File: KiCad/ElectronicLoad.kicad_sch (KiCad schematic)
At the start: 180 parts, among them J1 LOAD, J2 SMA2, J3 SMA1, J4 12V, J5 USB, J6 PROG, M1 FAN, Q1 any, Q2 any, Q3 BSS138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

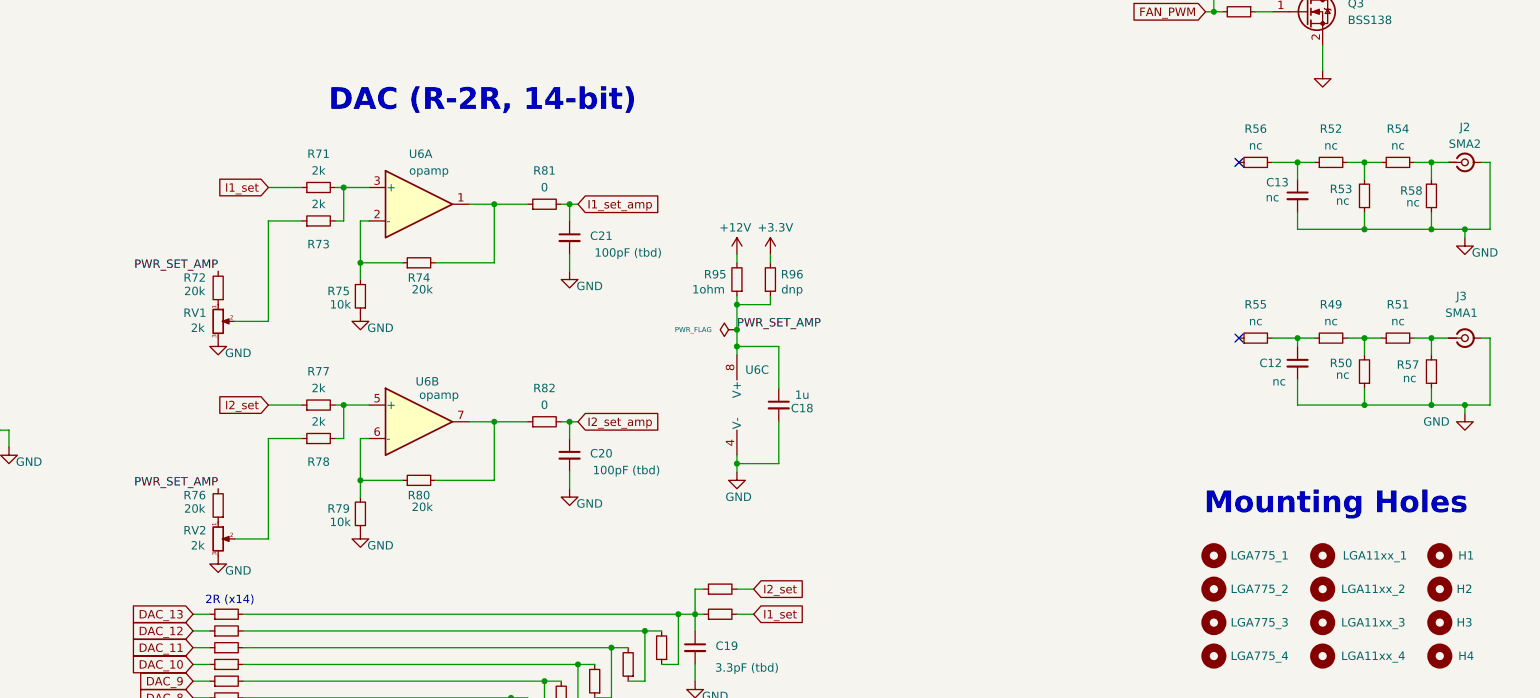
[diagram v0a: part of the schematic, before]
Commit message: rev0.2: remove DAC offset compensation and test connectors
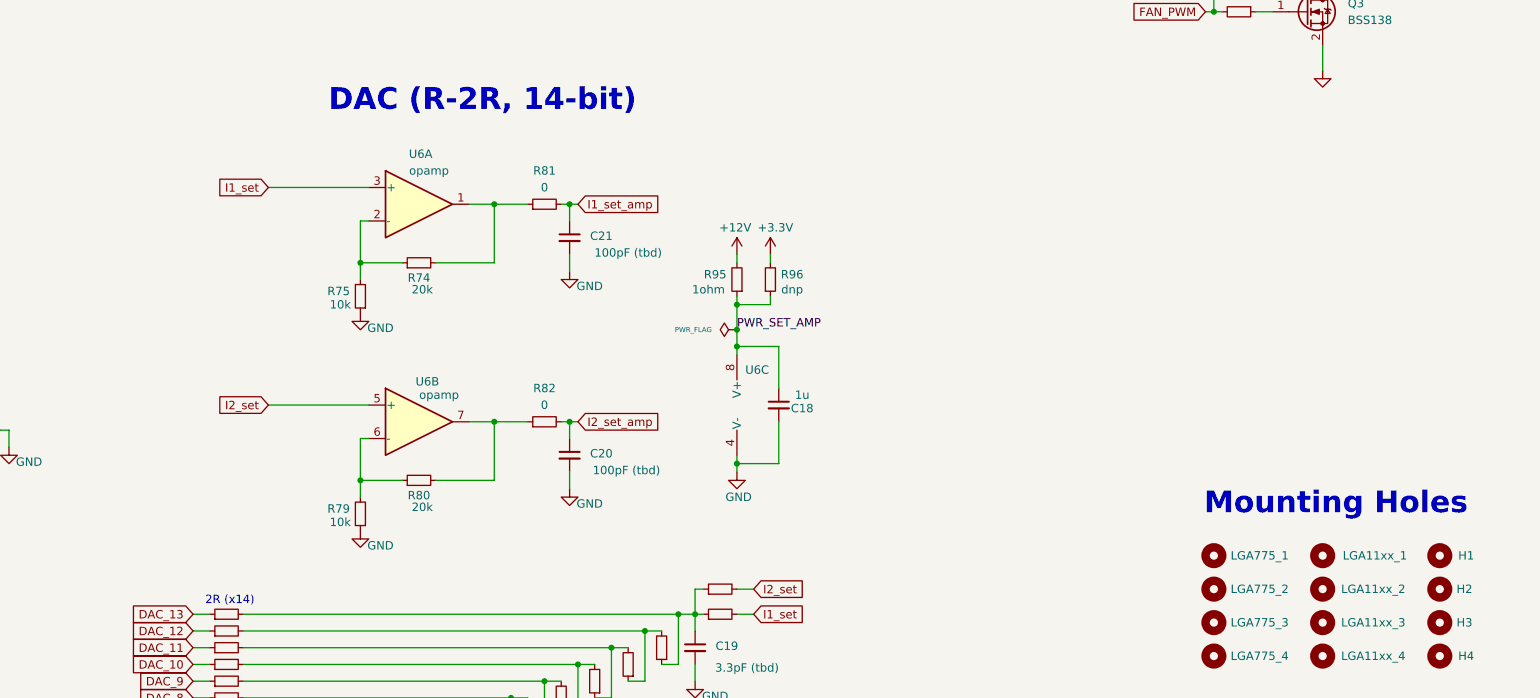
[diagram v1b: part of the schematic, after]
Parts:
- removed C12, C13: nc, Capacitor_SMD:C_0805_2012Metric, symbol Device:C_Small
- removed J2: SMA2, Library:SMA_Amphenol_901-143_Horizontal, symbol Connector:Conn_Coaxial_Small
- removed J3: SMA1, Library:SMA_Amphenol_901-143_Horizontal, symbol Connector:Conn_Coaxial_Small
- removed R49, R50, R51, R52, R53, R54, R55, R56, R57, R58: nc, Resistor_SMD:R_0805_2012Metric, symbol Device:R_Small
- removed R71, R73, R77, R78: 2k, Resistor_SMD:R_0603_1608Metric, symbol Device:R_Small
- removed R72, R76: 20k, Resistor_SMD:R_0603_1608Metric, symbol Device:R_Small
- removed RV1, RV2: 2k, Library-RV:PVG3A, symbol Device:R_Potentiometer_Small
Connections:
- net I1_set: now also U6.3 (+)
- net I2_set: now also U6.5 (+)
- no-connect marks 13 -> 11

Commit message: rev0.2: use only one Current Set line
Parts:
- removed C20: 100pF (tbd), Capacitor_SMD:C_0603_1608Metric, symbol Device:C_Small
- removed D10: 12V, Diode_SMD:D_SOD-323_HandSoldering, symbol Device:D_TVS_Small
- removed R41: 1k, Resistor_SMD:R_0603_1608Metric, symbol Device:R_Small
- removed R43, R82: 0, Resistor_SMD:R_0603_1608Metric, symbol Device:R_Small
- removed R79: 10k, Resistor_SMD:R_0603_1608Metric, symbol Device:R_Small
- removed R80: 20k, Resistor_SMD:R_0603_1608Metric, symbol Device:R_Small
- removed R92: R_Small, Resistor_SMD:R_0603_1608Metric, symbol Device:R_Small
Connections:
- net I2_set_a is gone; now on net I_set_a: U2.5 (+)
- net I1_set renamed I_set
- net I1_set_a renamed I_set_a
- net I1_set_amp renamed I_set_amp
- net I2_set: no longer names the net of U6.5 (+)
- no-connect marks 11 -> 14

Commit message: rev0.2: separate DAC10/11 lines from RX/TX
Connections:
- net DAC_10: now also U5.21 (GPIO13/TOUCH13/ADC2_CH2/FSPIQ/FSPIIO7); no longer J6.3 (Pin_3), U5.36 (U0RXD/GPIO44/CLK_OUT2)
- net DAC_11: now also U5.20 (GPIO12/TOUCH12/ADC2_CH1/FSPICLK/FSPIIO6); no longer J6.2 (Pin_2), U5.37 (U0TXD/GPIO43/CLK_OUT1)
- new net RX: J6.3 (Pin_3), U5.36 (U0RXD/GPIO44/CLK_OUT2)
- new net TX: J6.2 (Pin_2), U5.37 (U0TXD/GPIO43/CLK_OUT1)
- no-connect marks 14 -> 12
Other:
- moved on the sheet: C21, R74, R75, R81, U6A, U6B

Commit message: rev0.2: remove MOSFET caps
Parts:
- removed C14, C15: dnp*, Capacitor_SMD:C_0603_1608Metric, symbol Device:C_Small
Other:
- note added: "*div by 48"
- moved on the sheet: C18, C21, D13, D3, R11, R64, R74, R75, R81, R90, R95, R96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

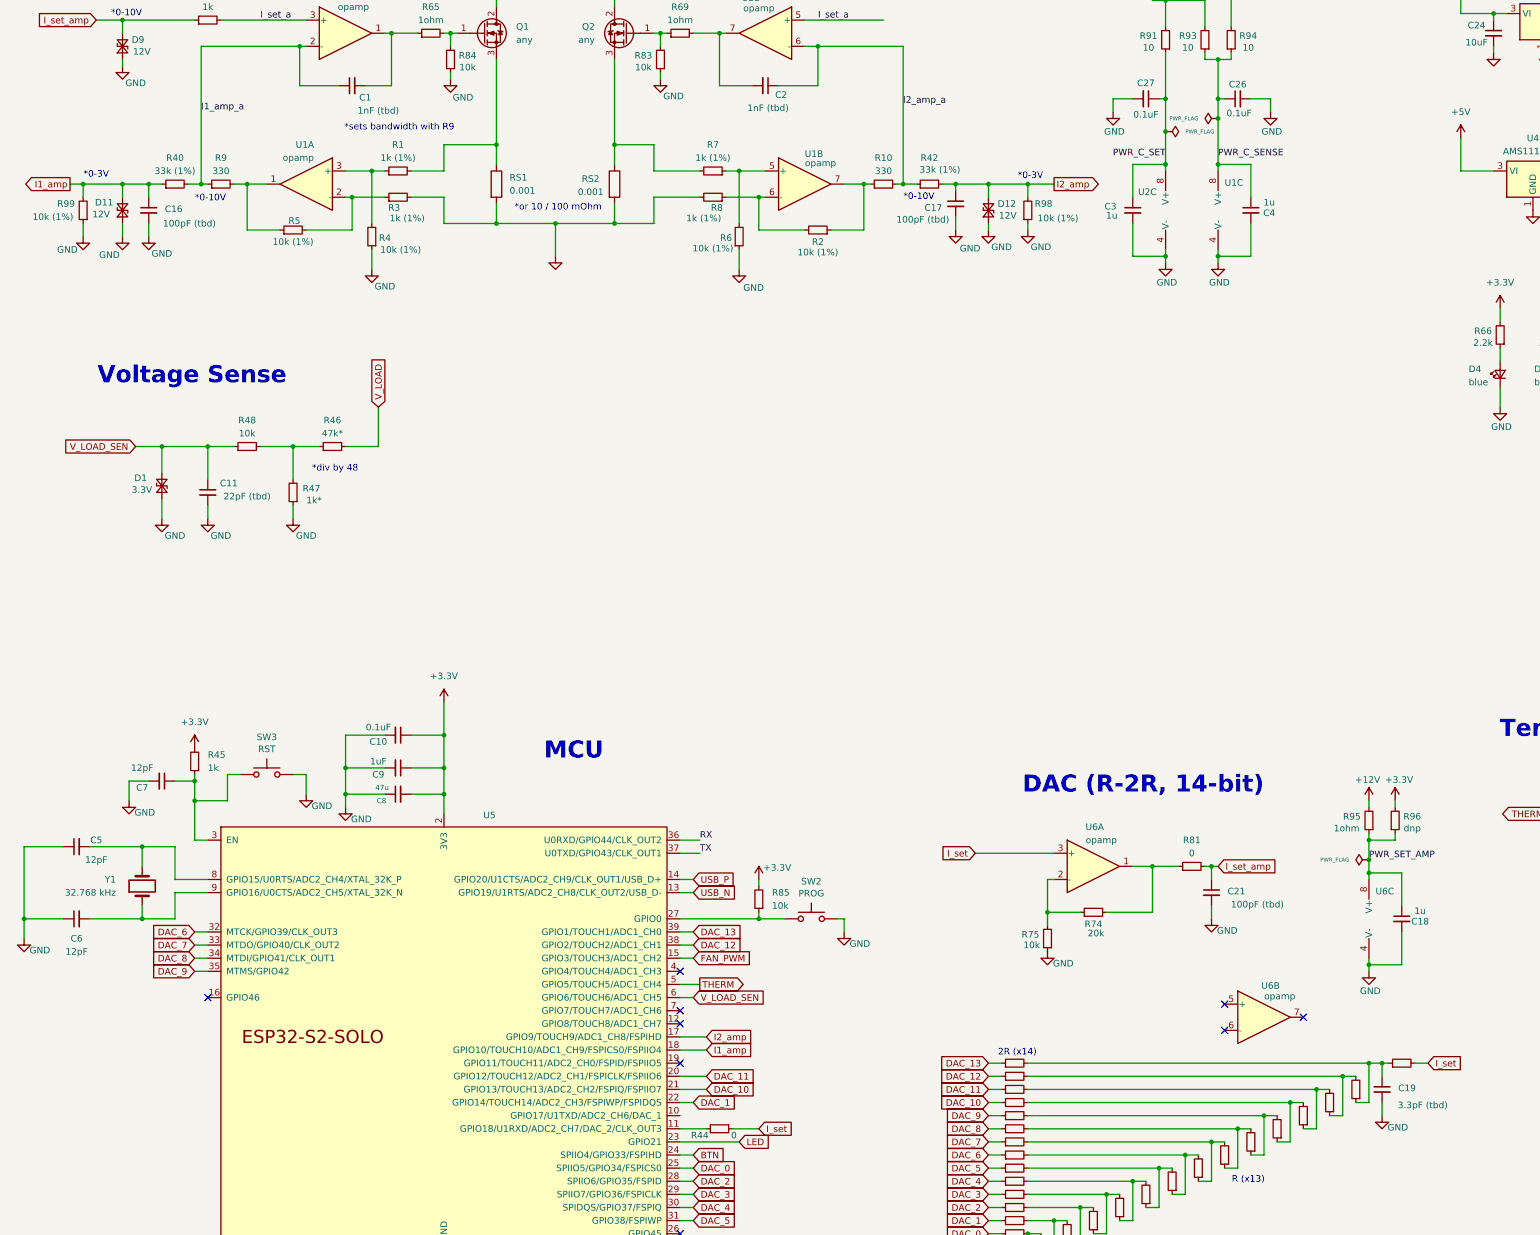
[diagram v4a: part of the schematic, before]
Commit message: rev0.2: redesign the Voltage & (MCU) Current Sense circuits
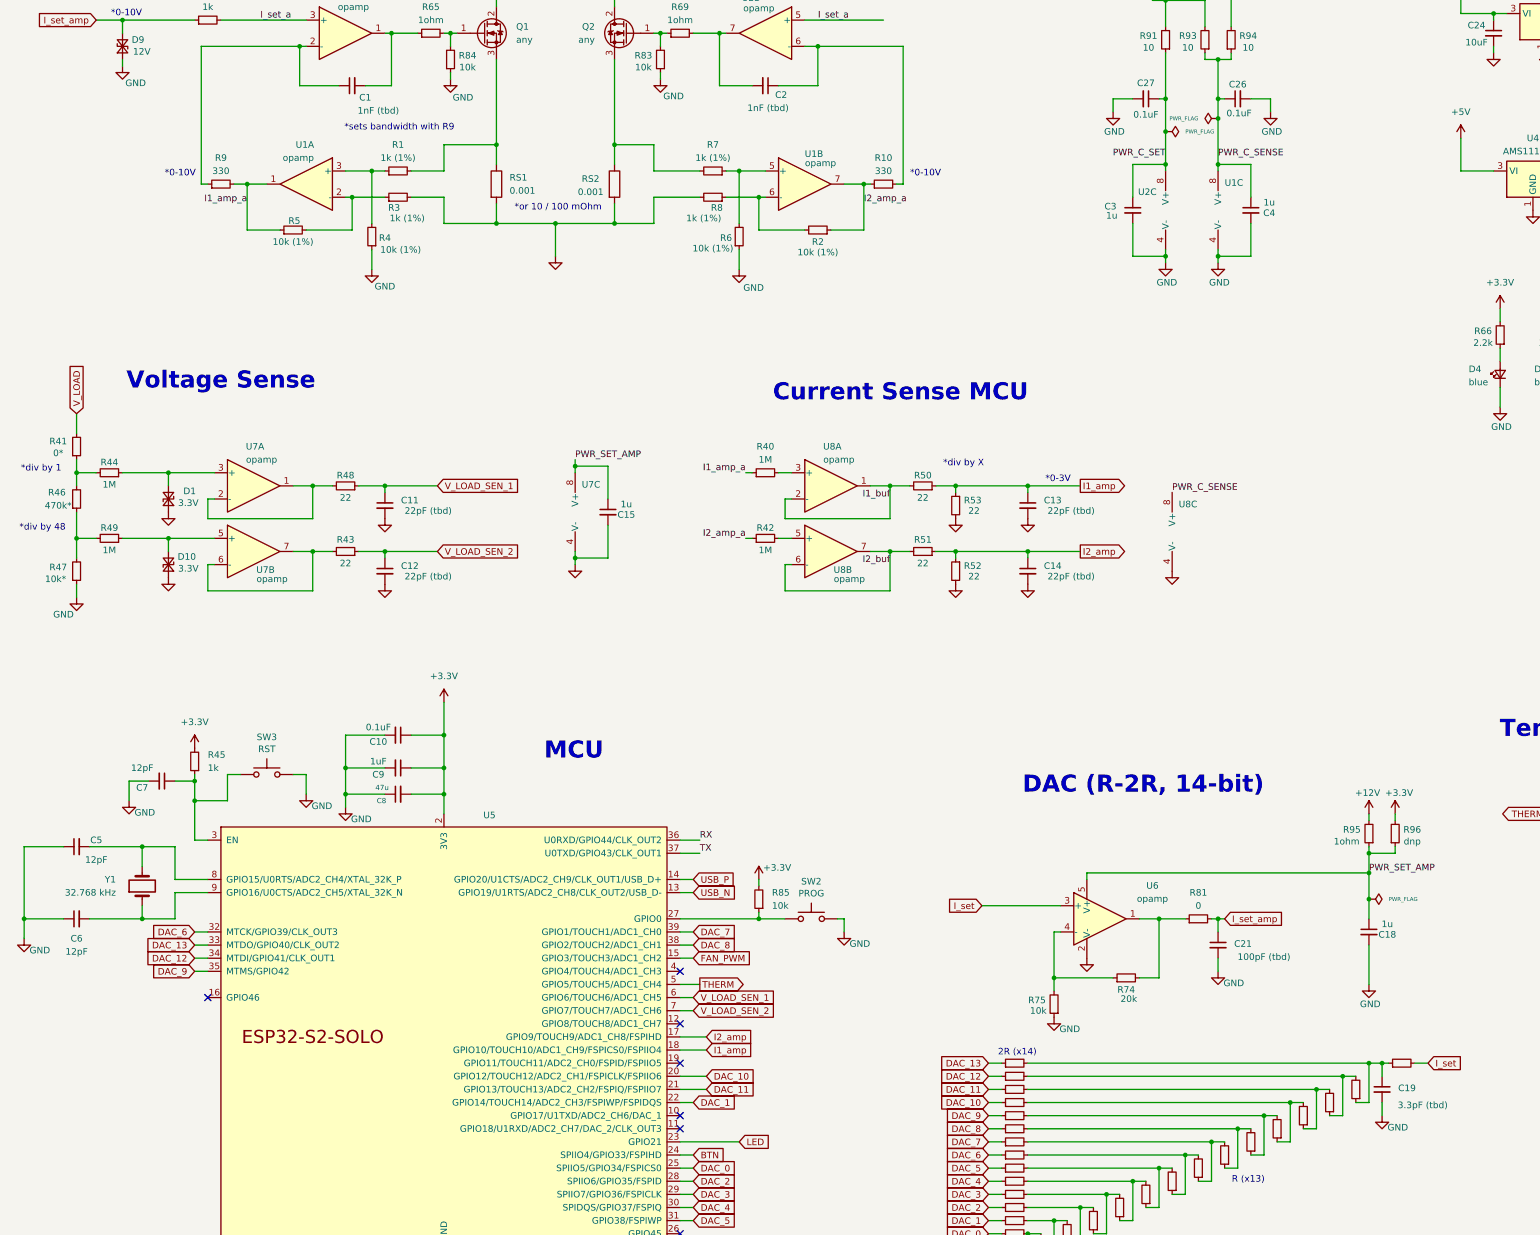
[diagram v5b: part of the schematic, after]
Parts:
- removed C16, C17: 100pF (tbd), Capacitor_SMD:C_0603_1608Metric, symbol Device:C_Small
- removed D11, D12: 12V, Diode_SMD:D_SOD-323_HandSoldering, symbol Device:D_TVS_Small
- removed R98, R99: 10k (1%), Resistor_SMD:R_0603_1608Metric, symbol Device:R_Small
- removed U6: opamp, Package_SO:SOIC-8_3.9x4.9mm_P1.27mm, symbol Amplifier_Operational:LM2904
- added C12, C13, C14: 22pF (tbd), Capacitor_SMD:C_0603_1608Metric, symbol Device:C_Small
- added C15: 1u, Capacitor_SMD:C_0603_1608Metric, symbol Device:C_Small
- added D10: 3.3V, Diode_SMD:D_SOD-323_HandSoldering, symbol Device:D_TVS_Small
- added R41: 0*, Resistor_SMD:R_0603_1608Metric, symbol Device:R_Small
- added R43, R50, R51, R52, R53: 22, Resistor_SMD:R_0603_1608Metric, symbol Device:R_Small
- added R49: 1M, Resistor_SMD:R_0603_1608Metric, symbol Device:R_Small
- added U6: opamp, Package_TO_SOT_SMD:SOT-23-5, symbol Amplifier_Operational:LMH6702MF
- added U7, U8: opamp, Package_SO:SOIC-8_3.9x4.9mm_P1.27mm, symbol Amplifier_Operational:LM2904
- C11: footprint Capacitor_SMD:C_0805_2012Metric -> Capacitor_SMD:C_0603_1608Metric
- R40, R42: value 33k (1%) -> 1M
- R44: value 0 -> 1M
- R46: value 47k* -> 470k*; footprint Resistor_SMD:R_0805_2012Metric -> Resistor_SMD:R_0603_1608Metric
- R47: value 1k* -> 10k*; footprint Resistor_SMD:R_0805_2012Metric -> Resistor_SMD:R_0603_1608Metric
- R48: value 10k -> 22; footprint Resistor_SMD:R_0805_2012Metric -> Resistor_SMD:R_0603_1608Metric
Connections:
- net DAC_10: now also U5.20 (GPIO12/TOUCH12/ADC2_CH1/FSPICLK/FSPIIO6); no longer U5.21 (GPIO13/TOUCH13/ADC2_CH2/FSPIQ/FSPIIO7)
- net DAC_11: now also U5.21 (GPIO13/TOUCH13/ADC2_CH2/FSPIQ/FSPIIO7); no longer U5.20 (GPIO12/TOUCH12/ADC2_CH1/FSPICLK/FSPIIO6)
- net DAC_12: now also U5.34 (MTDI/GPIO41/CLK_OUT1); no longer U5.38 (GPIO2/TOUCH2/ADC1_CH1)
- net DAC_13: now also U5.33 (MTDO/GPIO40/CLK_OUT2); no longer U5.39 (GPIO1/TOUCH1/ADC1_CH0)
- net DAC_7: now also U5.39 (GPIO1/TOUCH1/ADC1_CH0); no longer U5.33 (MTDO/GPIO40/CLK_OUT2)
- net DAC_8: now also U5.38 (GPIO2/TOUCH2/ADC1_CH1); no longer U5.34 (MTDI/GPIO41/CLK_OUT1)
- net GND: now also C12.2, C13.2, C14.2, C15.2, D10.1 (A1), R52.2, R53.2, U6.2 (V-), U7.4 (V-), U8.4 (V-)
- net I1_amp: now also C13.1, R50.1, R53.1; no longer R40.1
- net I1_amp_a: now also R40.1, R5.1, R9.2, U1.1; no longer C1.1, R40.2, R9.1, U2.2 (-)
- net I2_amp: now also C14.1, R51.1, R52.1; no longer R42.2
- net I2_amp_a: now also R10.1, R2.1, U1.7; no longer C2.1, R10.2, U2.6 (-)
- net I_set: now also U6.3 (+); no longer R44.1
- net PWR_C_SENSE: now also U8.8 (V+)
- net PWR_SET_AMP: now also C15.1, U6.5 (V+), U7.8 (V+)
- net V_LOAD: now also R41.2; no longer R46.2
- net at R46.1, R47.2: now also R49.2; no longer R48.2
- net at R74.1, R75.2: now also U6.4 (-)
- net at R74.2, R81.1: now also U6.1
- net at R44.2: now also R46.2, R41.1; no longer U5.11 (GPIO18/U1RXD/ADC2_CH7/DAC_2/CLK_OUT3)
- net V_LOAD_SEN_2: now reaches U5.7 (GPIO7/TOUCH7/ADC1_CH6)
- net V_LOAD_SEN_2: now also C12.1, R43.1
- net V_LOAD_SEN renamed V_LOAD_SEN_1
- net V_LOAD_SEN_1: no longer D1.2 (A2)
- new net: R48.2, U7.1, U7.2 (-)
- new net: D1.2 (A2), R44.1, U7.3 (+)
- new net: R42.2, U8.5 (+)
- new net: R40.2, U8.3 (+)
- new net: C1.1, R9.1, U2.2 (-)
- new net: D10.2 (A2), R49.1, U7.5 (+)
- new net: R43.2, U7.6 (-), U7.7
- new net: C2.1, R10.2, U2.6 (-)
- new net I1_buf: R50.2, U8.1, U8.2 (-)
- new net I2_buf: R51.2, U8.6 (-), U8.7
- no-connect marks 12 -> 10
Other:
- note added: "*div by 1"
- note added: "*div by X"
- note added: "Current Sense MCU"
- moved on the sheet: C11, C18, C21, D1, R40, R42, R46, R47, R48, R74, R75, R81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

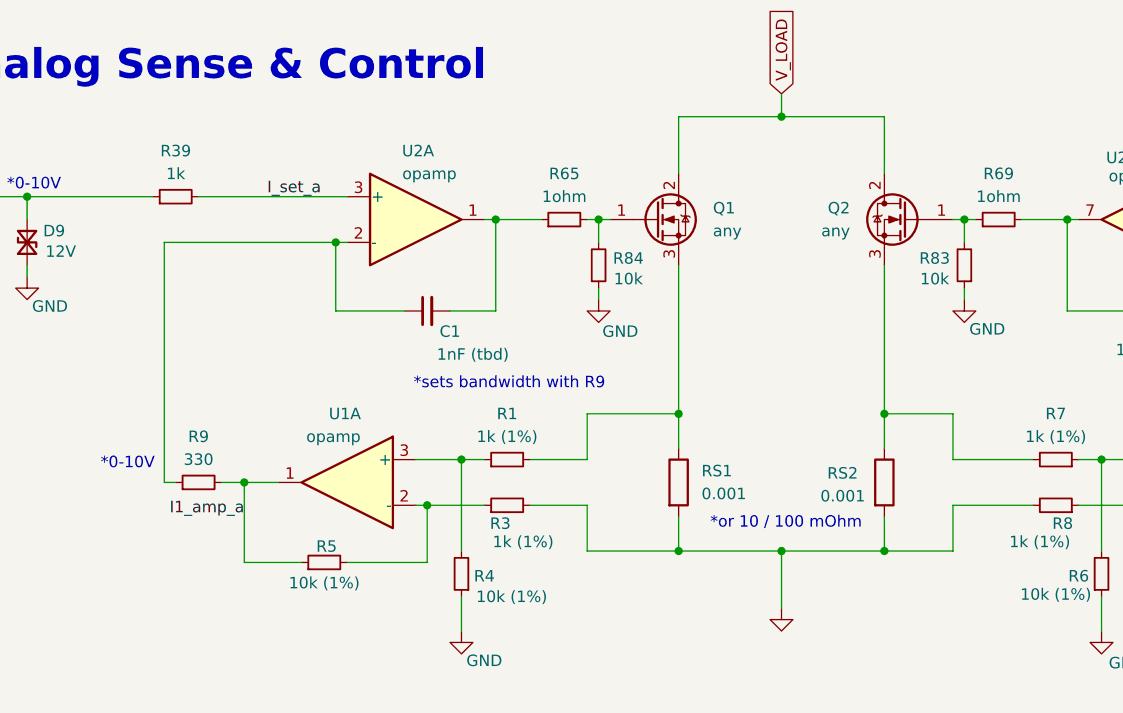
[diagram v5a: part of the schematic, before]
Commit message: rev0.2: add duplicate current sense resistor footprint
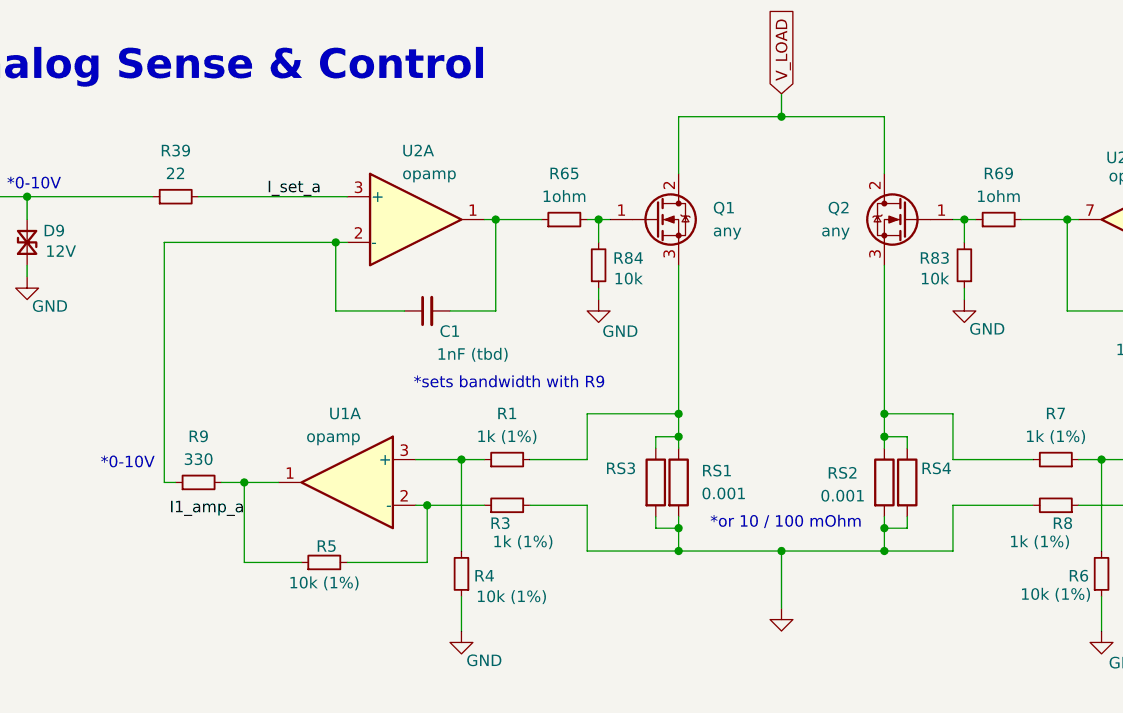
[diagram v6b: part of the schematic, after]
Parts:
- added RS3, RS4: 0.001, Resistor_SMD:R_2512_6332Metric, symbol Device:R
- R39: value 1k -> 22
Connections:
- net GND: now also RS3.2, RS4.2
- net at Q1.3 (S), R1.2, RS1.1: now also RS3.1
- net at Q2.3 (S), R7.2, RS2.1: now also RS4.1
